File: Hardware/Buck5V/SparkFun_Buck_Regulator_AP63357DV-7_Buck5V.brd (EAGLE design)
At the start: 25.4 x 25.4 mm, 54 parts, among them J3 POWER_JACK, U1 AP63357

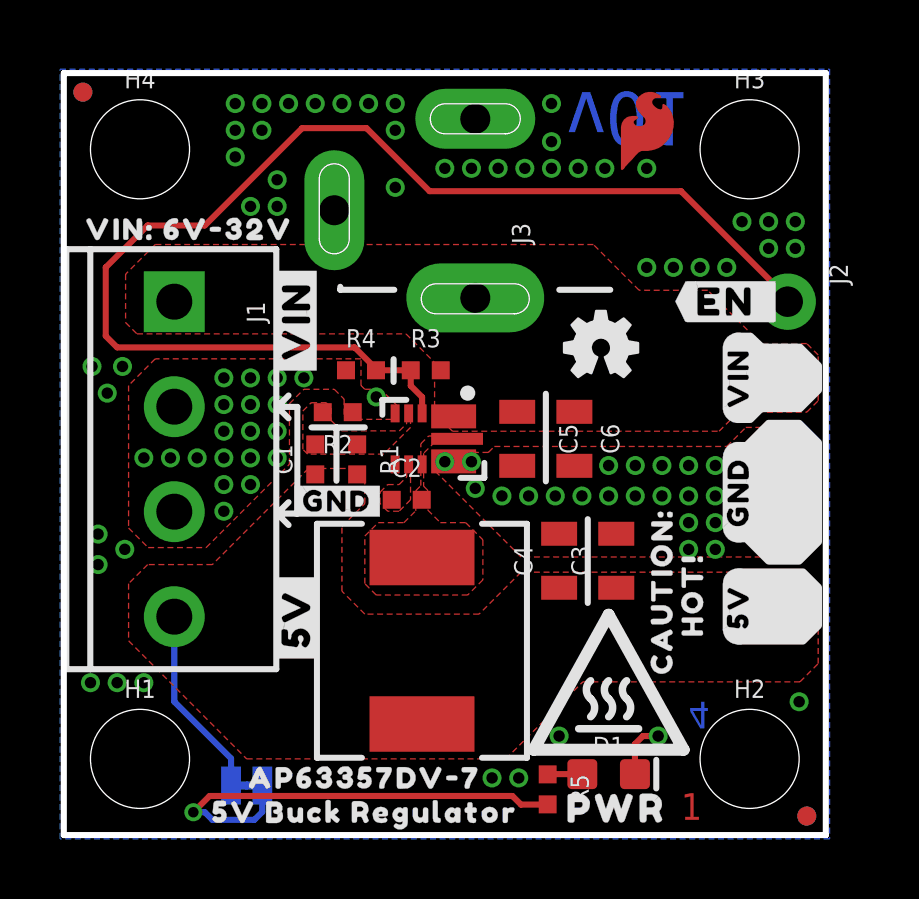
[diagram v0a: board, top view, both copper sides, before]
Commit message: Ready for v10 reds.
1x1 - Thicken silk border on U1
micro - Move fiducial to increase heat sink size
both - panelize
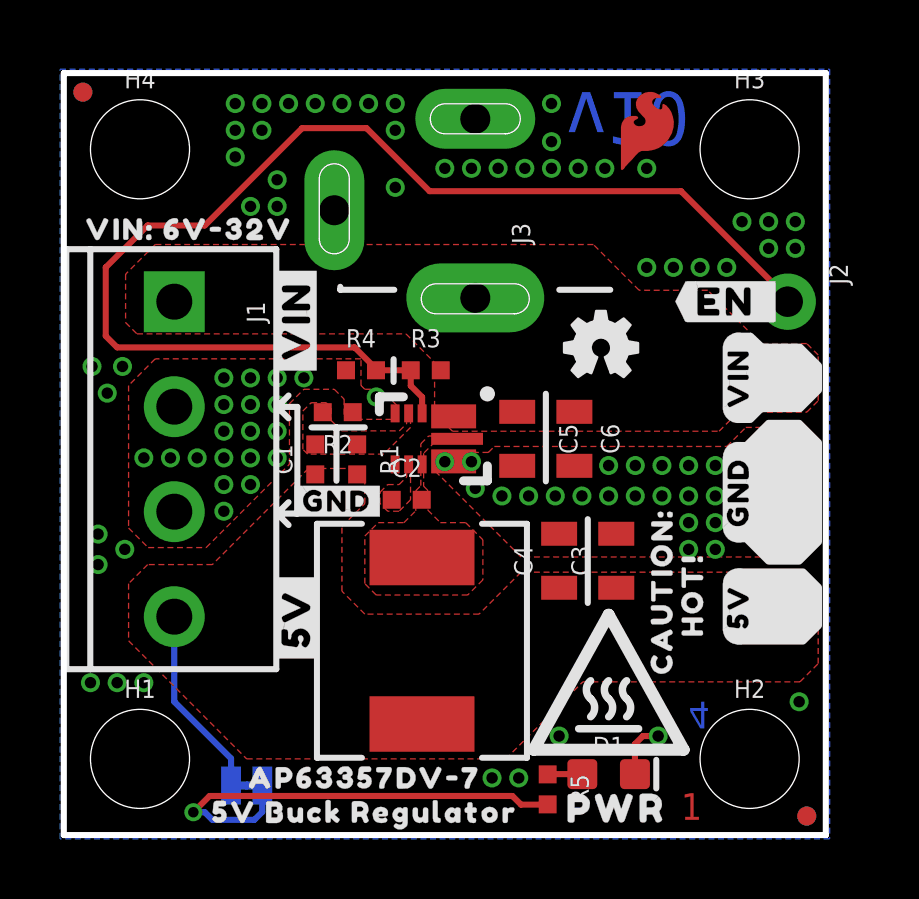
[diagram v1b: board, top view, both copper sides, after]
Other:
- board text added: "v10"
- board text removed: "v01"
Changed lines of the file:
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@@
 <wire x1="0" y1="25.4" x2="0" y2="0" width="0.2032" layer="20"/>
 <rectangle x1="6.35" y1="2.159" x2="21.59" y2="14.859" layer="30" rot="R90"/>
-<text x="16.764" y="24.765" size="1.778" layer="16" font="vector" ratio="15" rot="SMR180">v01</text>
+<text x="16.764" y="24.765" size="1.778" layer="16" font="vector" ratio="15" rot="SMR180">v10</text>
 <text x="20.574" y="0.508" size="0.889" layer="1" font="vector" ratio="15">1</text>
 <text x="20.066" y="0.508" size="0.889" layer="2" font="vector" ratio="15">2</text>
@@
 <element name="FRAME1" library="SparkFun-Aesthetics" package="CREATIVE_COMMONS" value="FRAME-LEDGER" x="21.209" y="-16.383" smashed="yes">
 <attribute name="DESIGNER" value="Alex Brudner" x="21.209" y="-16.383" size="1.778" layer="27" display="off"/>
-<attribute name="REV" value="v01" x="21.209" y="-16.383" size="1.778" layer="27" display="off"/>
+<attribute name="REV" value="v10" x="21.209" y="-16.383" size="1.778" layer="27" display="off"/>
 </element>
 <element name="FD1" library="SparkFun-Aesthetics" package="FIDUCIAL-MICRO" value="FIDUCIALUFIDUCIAL" x="24.765" y="0.635" smashed="yes"/>

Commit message: Prepare for v10 reds order.
Change R1/R2 to better match 5V output requirement.
Repanelize.
Reorganize Production Folder Structure.
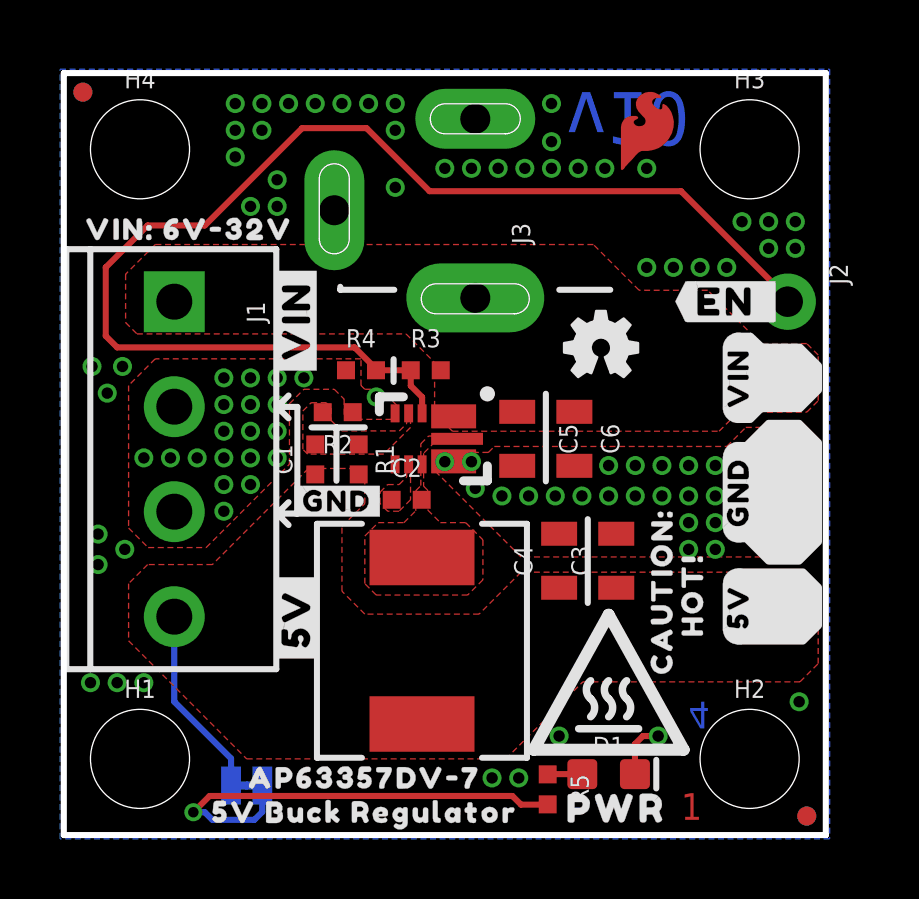
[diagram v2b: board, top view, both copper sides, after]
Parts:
- R1: value 150k -> 220K
- R2: value 28.7k -> 41.2K
- moved R1 0.05 mm to (9.83, 12.5)
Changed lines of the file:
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@@
 <attribute name="VALUE" x="22.098" y="19.05" size="0.6096" layer="27" font="vector" ratio="20" rot="R270"/>
 </element>
-<element name="R2" library="Buck5V" package="0402-TIGHT" value="28.7k" x="9.1313" y="14.097" smashed="yes" rot="R180">
+<element name="R2" library="Buck5V" package="0402-TIGHT" value="41.2K" x="9.1313" y="14.097" smashed="yes" rot="R180">
 <attribute name="NAME" x="9.1313" y="13.335" size="0.6096" layer="25" font="vector" ratio="20" rot="R180" align="bottom-center"/>
-<attribute name="PN" value="RT0402FRE0728K7L" x="9.1313" y="14.097" size="1.778" layer="27" rot="R180" display="off"/>
-<attribute name="PROD_ID" value="RES-17225" x="9.1313" y="14.097" size="1.778" layer="27" rot="R180" display="off"/>
-<attribute name="VALUE" value="28.7k" x="9.1313" y="14.859" size="0.6096" layer="27" font="vector" ratio="20" rot="R180" align="top-center"/>
+<attribute name="PN" value="RC0402FR-0741K2L" x="9.1313" y="14.097" size="1.778" layer="27" rot="R180" display="off"/>
+<attribute name="PROD_ID" value="RES-15010" x="9.1313" y="14.097" size="1.778" layer="27" rot="R180" display="off"/>
+<attribute name="VALUE" value="41.2K" x="9.1313" y="14.859" size="0.6096" layer="27" font="vector" ratio="20" rot="R180" align="top-center"/>
 </element>
 <element name="U1" library="Buck5V" package="V-DFN3020-13" value="AP63357" x="12.319" y="13.208" smashed="yes" rot="R180">
 <attribute name="PN" value="AP63357DV-7" x="12.319" y="13.208" size="1.778" layer="27" rot="R180" display="off"/>
 <attribute name="PROD_ID" value="VREG-17224" x="12.319" y="13.208" size="1.778" layer="27" rot="R180" display="off"/>
-</element>
-<element name="R1" library="SparkFun-Resistors" package="0402-TIGHT" value="150k" x="9.779" y="12.5222" smashed="yes" rot="R270">
-<attribute name="NAME" x="10.541" y="12.5222" size="0.6096" layer="25" font="vector" ratio="20" rot="R270" align="bottom-center"/>
-<attribute name="PROD_ID" value="RES-15093" x="9.779" y="12.5222" size="1.778" layer="27" rot="R270" display="off"/>
-<attribute name="RES" value="150k" x="9.779" y="12.5222" size="1.778" layer="27" rot="R270" display="off"/>
 </element>
 <element name="C1" library="SparkFun-Capacitors" package="0402-TIGHT" value="47pF" x="8.382" y="12.5222" smashed="yes" rot="R90">
@@
 <element name="U$11" library="output" package="6V#32V10" value="" x="8.001" y="17.78" smashed="yes" rot="MR180"/>
 <element name="U$12" library="output" package="HOT##0" value="" x="20.955" y="8.001" smashed="yes" rot="R90"/>
+<element name="R1" library="SparkFun-Resistors" package="0402-TIGHT" value="220K" x="9.8298" y="12.5222" smashed="yes" rot="R270">
+<attribute name="NAME" x="10.3918" y="12.5222" size="0.6096" layer="25" font="vector" ratio="20" rot="R270" align="bottom-center"/>
+<attribute name="PROD_ID" value="RES-15094" x="9.8298" y="12.5222" size="1.778" layer="27" rot="R270" display="off"/>
+<attribute name="VALUE" x="9.2678" y="12.5222" size="0.6096" layer="27" font="vector" ratio="20" rot="R270" align="top-center"/>
+</element>
 </elements>
 <signals>
 <signal name="FB">
 <contactref element="U1" pad="P$3"/>
-<contactref element="R1" pad="1"/>
 <contactref element="R2" pad="2"/>
 <contactref element="C1" pad="2"/>
@@
 <vertex x="11.43" y="13.716"/>
 </polygon>
+<contactref element="R1" pad="1"/>
 </signal>
 <signal name="SW">
@@
 </signal>
 <signal name="5V">
-<contactref element="R1" pad="2"/>
 <contactref element="C1" pad="1"/>
 <contactref element="L1" pad="P$2"/>
@@
 <wire x1="3.683" y1="4.445" x2="3.683" y2="7.28" width="0.2032" layer="16"/>
 <wire x1="5.5753" y1="2.5527" x2="3.683" y2="4.445" width="0.2032" layer="16"/>
+<contactref element="R1" pad="2"/>
 </signal>
 <signal name="N$2">
